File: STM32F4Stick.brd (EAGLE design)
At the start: 46.7 x 25.9 mm, 46 parts, among them U1 MIC5219 3.3V, U2 USD-SOCKETNEW

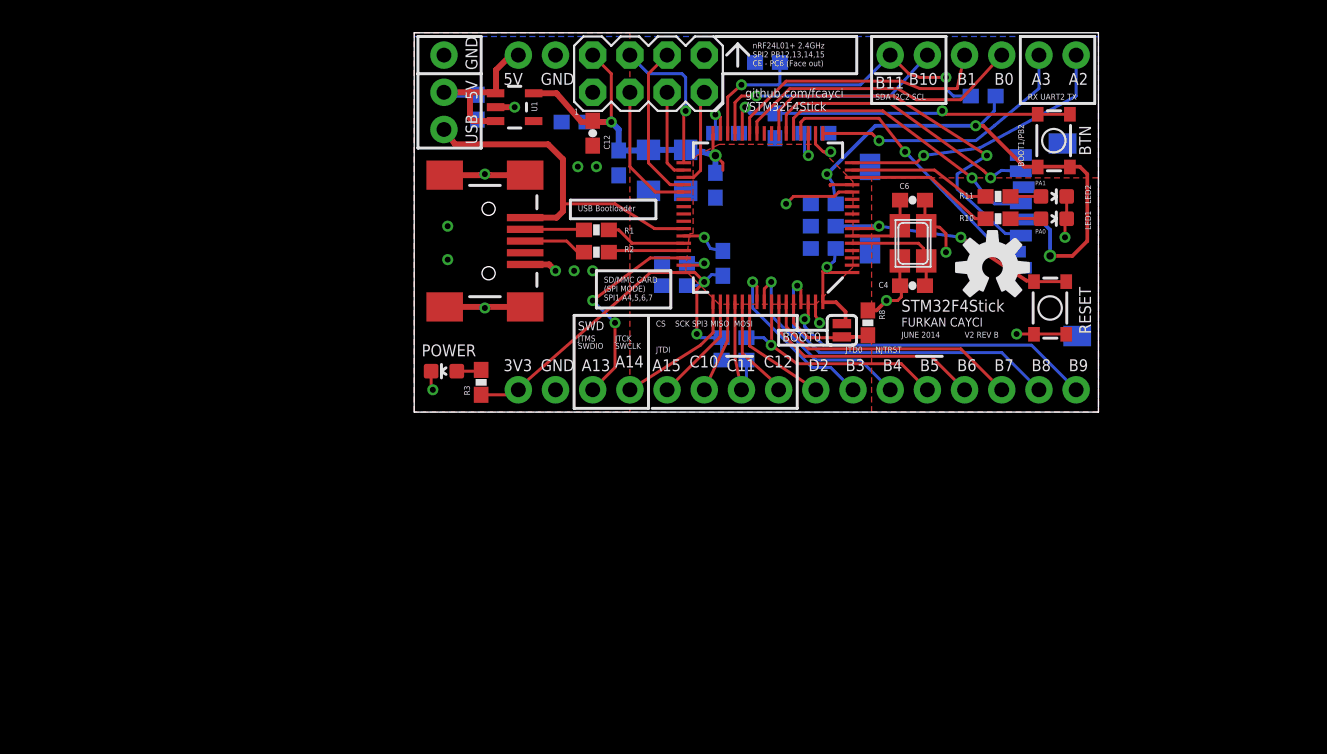
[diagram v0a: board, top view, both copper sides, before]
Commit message: version 3 still in development. playing with mpu6050/9150 module to see if one can fit
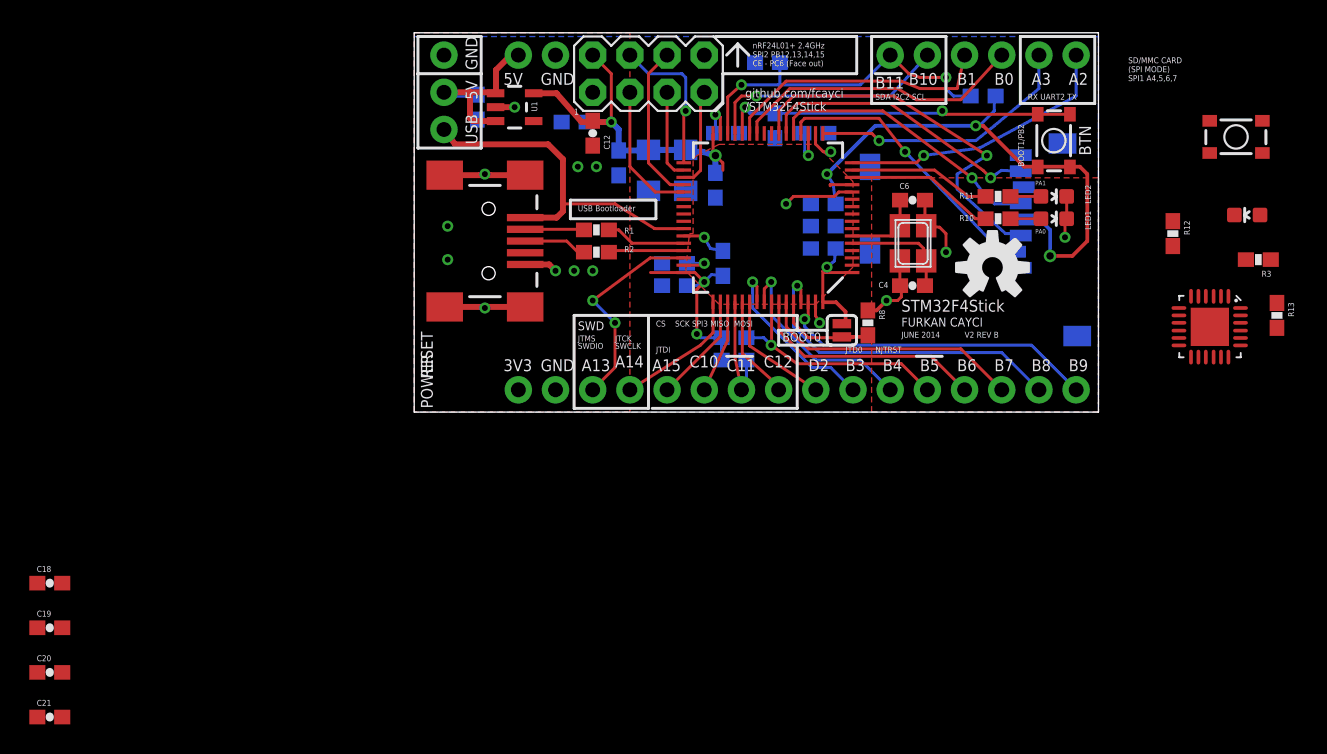
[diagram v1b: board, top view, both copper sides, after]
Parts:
- added C18, C19, C20, C21: 0.1uF, SparkFun-Capacitors:0603-CAP
- added R12, R13: 4.7K, SparkFun-Resistors:0603-RES
- added U3: MPU-6000QFN-24, SparkFun-Sensors:QFN-24-TESTING
- moved D1 55.9 mm to (56.9, 13.5)
- moved R3 53.7 mm to (57.7, 10.4), turned to 180 degrees
- moved S1 17.3 mm to (56.1, 18.8), turned to 180 degrees
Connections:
- new net SCL: R12.2, U3.23
- new net SDA: R13.2, U3.24
- net GND: now also U3.18
- net VCC: now also R12.1, R13.1, U3.13, U3.9
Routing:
- net NRST: track 18.6 -> 0.00 mm, vias 2 -> 0
- net VCC: track 106.2 -> 91.6 mm
- net GND: track 40.9 -> 36.3 mm, vias 18 -> 16
- net N$35: track 1.70 -> 0.00 mm
